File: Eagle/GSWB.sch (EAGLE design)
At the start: 14 parts

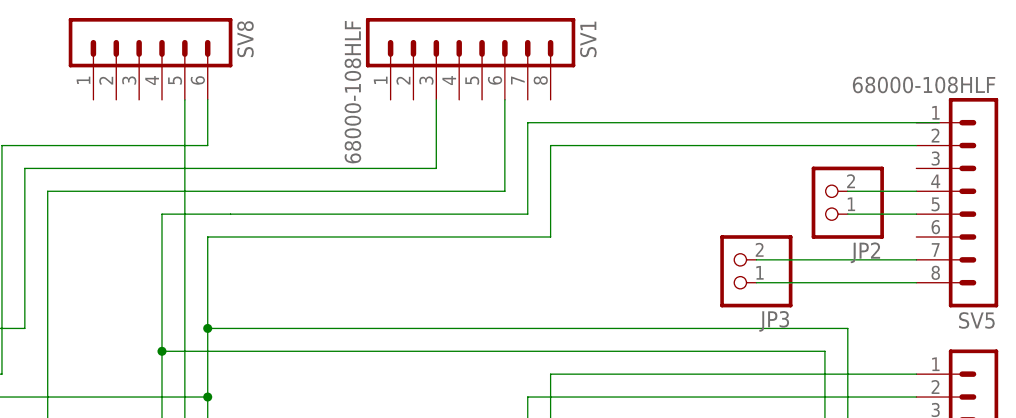
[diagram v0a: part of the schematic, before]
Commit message: updated Gerber files
Added trace from lbat to D10
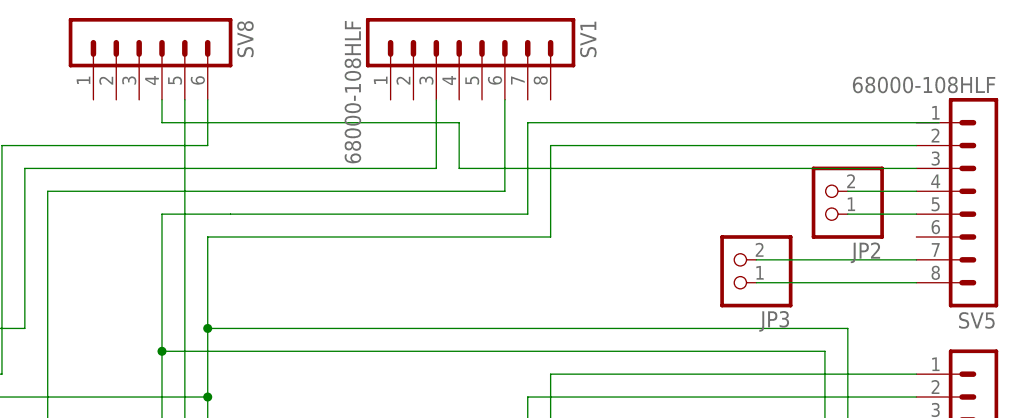
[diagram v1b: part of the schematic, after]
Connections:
- new net N$15: SV5.3, SV8.4
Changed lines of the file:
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@@
+</segment>
+</net>
+<net name="N$15" class="0">
+<segment>
+<pinref part="SV5" gate="1" pin="3"/>
+<wire x1="137.16" y1="93.98" x2="86.36" y2="93.98" width="0.1524" layer="91"/>
+<wire x1="86.36" y1="93.98" x2="86.36" y2="99.06" width="0.1524" layer="91"/>
+<pinref part="SV8" gate="1" pin="4"/>
+<wire x1="86.36" y1="99.06" x2="53.34" y2="99.06" width="0.1524" layer="91"/>
+<wire x1="53.34" y1="99.06" x2="53.34" y2="101.6" width="0.1524" layer="91"/>
 </segment>
 </net>

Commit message: Adding CAD Files
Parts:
- R4: value RC1206FR-07100RL -> RT1210BRD07150RL
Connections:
- net EN_GND: now also SV5.1
- net GND: now also SV2.3, SV5.2
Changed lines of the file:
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@@
 <part name="R2" library="rcl" deviceset="R-US_" device="M1206" value="RC1206FR-07100RL"/>
 <part name="R3" library="rcl" deviceset="R-US_" device="M1206" value="RC1206FR-07100RL"/>
-<part name="R4" library="rcl" deviceset="R-US_" device="M1206" value="RC1206FR-07100RL"/>
+<part name="R4" library="rcl" deviceset="R-US_" device="M1206" value="RT1210BRD07150RL"/>
 <part name="SV5" library="con-lstb" deviceset="MA08-1" device="" value="68000-108HLF"/>
 <part name="SV6" library="con-lstb" deviceset="MA05-1" device=""/>
@@
 </segment>
 </net>
-<net name="N$8" class="0">
-<segment>
-<wire x1="60.96" y1="88.9" x2="93.98" y2="88.9" width="0.1524" layer="91"/>
-<wire x1="93.98" y1="88.9" x2="93.98" y2="99.06" width="0.1524" layer="91"/>
-<wire x1="93.98" y1="99.06" x2="139.7" y2="99.06" width="0.1524" layer="91"/>
-</segment>
-</net>
 <net name="EN_GND" class="0">
 <segment>
@@
 <wire x1="53.34" y1="73.66" x2="53.34" y2="53.34" width="0.1524" layer="91"/>
 <wire x1="53.34" y1="73.66" x2="53.34" y2="88.9" width="0.1524" layer="91"/>
-<wire x1="53.34" y1="88.9" x2="60.96" y2="88.9" width="0.1524" layer="91"/>
 <junction x="53.34" y="73.66"/>
 <pinref part="SV6" gate="G$1" pin="4"/>
@@
 <junction x="127" y="63.5"/>
 <pinref part="JP1" gate="G$1" pin="1"/>
+<wire x1="93.98" y1="88.9" x2="93.98" y2="99.06" width="0.1524" layer="91"/>
+<wire x1="93.98" y1="99.06" x2="137.16" y2="99.06" width="0.1524" layer="91"/>
+<pinref part="SV5" gate="1" pin="1"/>
+<wire x1="53.34" y1="88.9" x2="93.98" y2="88.9" width="0.1524" layer="91"/>
 </segment>
 </net>
@@
 <wire x1="0" y1="68.58" x2="58.42" y2="68.58" width="0.1524" layer="91"/>
 <junction x="58.42" y="68.58"/>
+<pinref part="SV2" gate="1" pin="3"/>
+<wire x1="55.88" y1="53.34" x2="55.88" y2="58.42" width="0.1524" layer="91"/>
+<wire x1="55.88" y1="58.42" x2="58.42" y2="58.42" width="0.1524" layer="91"/>
+<pinref part="SV5" gate="1" pin="2"/>
 </segment>
 </net>
